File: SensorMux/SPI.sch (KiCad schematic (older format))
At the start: 12 parts

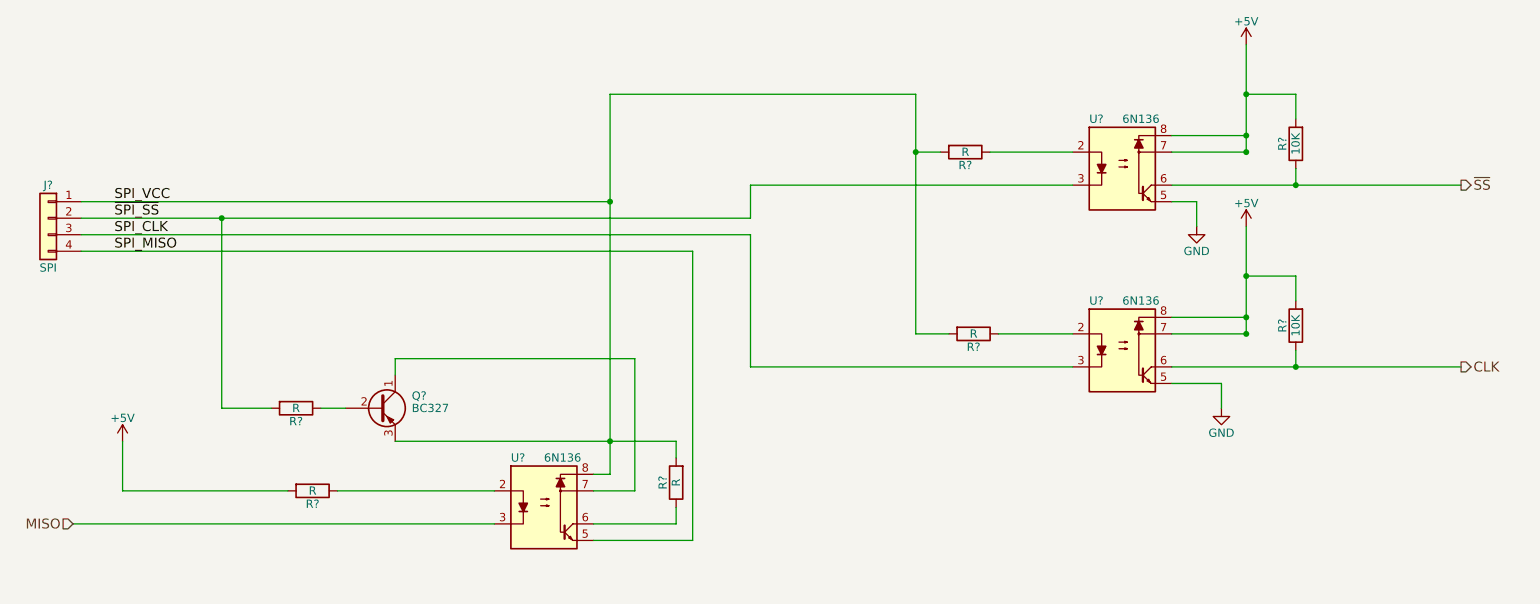
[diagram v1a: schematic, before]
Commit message: Working on adding analog part with SPI adjustment so the computer can control the opamps without needing manual trimpots.
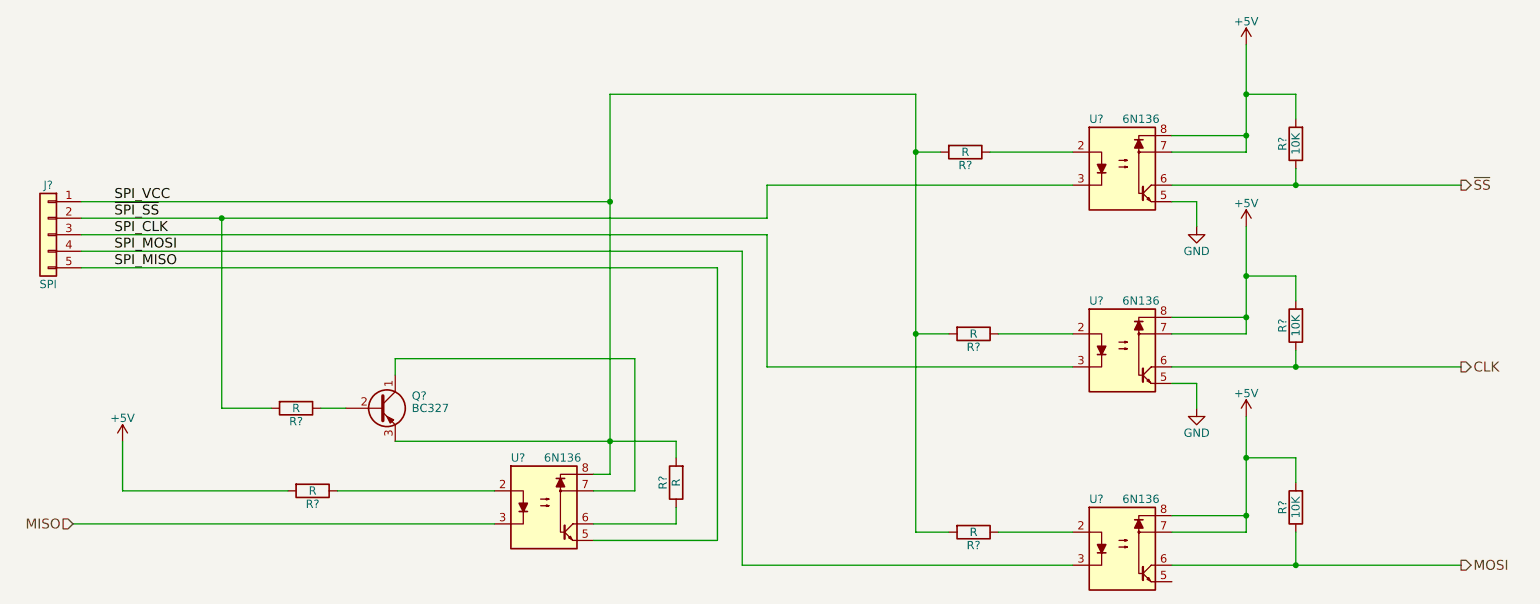
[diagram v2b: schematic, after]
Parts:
- removed J?: SPI, symbol Conn_01x04
- added J?: SPI, symbol Conn_01x05
- added R?: R, symbol R
- added R?: 10K, symbol R
- added U?: 6N136, Housings_DIP:DIP-8_W7.62mm, symbol 6N136
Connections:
- net +5V: now also R?.2, U?.7, U?.8
- net SPI_CLK: now also J?.3 (Pin_3)
- net SPI_MISO: now also J?.5 (Pin_5)
- net SPI_VCC: now also J?.1 (Pin_1), R?.2
- net ~SPI_SS: now also J?.2 (Pin_2)
- new net: R?.1, U?.2
- new net MOSI: R?.1, U?.6
- new net SPI_MOSI: J?.4 (Pin_4), U?.3
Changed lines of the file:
@@
-$EndComp
-$Comp
-L Conn_01x04 J?
-U 1 1 5A4AA249
-P 1700 3400
-F 0 "J?" H 1700 3600 50  0000 C CNN
-F 1 "SPI" H 1700 3100 50  0000 C CNN
-F 2 "" H 1700 3400 50  0001 C CNN
-F 3 "" H 1700 3400 50  0001 C CNN
-	1    1700 3400
-	-1   0    0    -1
 $EndComp
 $Comp
@@
 	-1   0    0    1
 $EndComp
-Text Label 2100 3600 0    60   ~ 0
+Text Label 2100 3700 0    60   ~ 0
 SPI_MISO
 $Comp
@@
 	7400 3000 7900 3000
 Wire Wire Line
-	5950 3200 7900 3200
+	6050 3200 7900 3200
 Wire Wire Line
 	1900 3300 5100 3300
@@
 	5100 2650 6950 2650
 Wire Wire Line
-	6950 2650 6950 4100
+	6950 2650 6950 5300
 Wire Wire Line
 	6950 4100 7150 4100
@@
 Connection ~ 6950 3000
 Wire Wire Line
-	5950 3400 5950 3200
-Wire Wire Line
-	1900 3400 5950 3400
-Wire Wire Line
-	1900 3500 5950 3500
-Wire Wire Line
-	5950 3500 5950 4300
-Wire Wire Line
-	5950 4300 7900 4300
+	6050 3400 6050 3200
+Wire Wire Line
+	1900 3400 6050 3400
+Wire Wire Line
+	1900 3500 6050 3500
+Wire Wire Line
+	6050 3500 6050 4300
+Wire Wire Line
+	6050 4300 7900 4300
 Wire Wire Line
 	3050 4550 2750 4550
@@
 	5500 5250 5500 5150
 Wire Wire Line
-	5000 5350 5600 5350
-Wire Wire Line
-	5600 5350 5600 3600
-Wire Wire Line
-	5600 3600 1900 3600
+	5000 5350 5750 5350
+Wire Wire Line
+	5750 5350 5750 3700
+Wire Wire Line
+	5750 3700 1900 3700
 Wire Wire Line
 	3450 5050 4400 5050
@@
 Wire Wire Line
 	8500 3200 10250 3200
-Connection ~ 8950 3000
 Wire Wire Line
 	8500 3300 8650 3300
@@
 L GND #PWR?
 U 1 1 5A4AAE1E
-P 8800 4550
-F 0 "#PWR?" H 8800 4300 50  0001 C CNN
-F 1 "GND" H 8800 4400 50  0000 C CNN
-F 2 "" H 8800 4550 50  0001 C CNN
-F 3 "" H 8800 4550 50  0001 C CNN
-	1    8800 4550
+P 8650 4550
+F 0 "#PWR?" H 8650 4300 50  0001 C CNN
+F 1 "GND" H 8650 4400 50  0000 C CNN
+F 2 "" H 8650 4550 50  0001 C CNN
+F 3 "" H 8650 4550 50  0001 C CNN
+	1    8650 4550
 	1    0    0    -1
 $EndComp
@@
 Wire Wire Line
 	8500 4300 10250 4300
-Connection ~ 8950 4100
-Wire Wire Line
-	8500 4400 8800 4400
-Wire Wire Line
-	8800 4400 8800 4550
+Wire Wire Line
+	8500 4400 8650 4400
+Wire Wire Line
+	8650 4400 8650 4550
 Wire Wire Line
 	8950 3450 8950 4100
@@
 Text HLabel 10250 4300 2    60   Output ~ 0
 CLK
+$Comp
+L Conn_01x05 J?
+U 1 1 5A5A91BD
+P 1700 3500
+F 0 "J?" H 1700 3800 50  0000 C CNN
+F 1 "SPI" H 1700 3200 50  0000 C CNN
+F 2 "" H 1700 3500 50  0001 C CNN
+F 3 "" H 1700 3500 50  0001 C CNN
+	1    1700 3500
+	-1   0    0    -1
+$EndComp
+Wire Wire Line
+	1900 3600 5900 3600
+Wire Wire Line
+	5900 3600 5900 5500
+$Comp
+L R R?
+U 1 1 5A5A9355
+P 7300 5300
+F 0 "R?" V 7380 5300 50  0000 C CNN
+F 1 "R" V 7300 5300 50  0000 C CNN
+F 2 "" V 7230 5300 50  0001 C CNN
+F 3 "" H 7300 5300 50  0001 C CNN
+	1    7300 5300
+	0    1    1    0
+$EndComp
+$Comp
+L 6N136 U?
+U 1 1 5A5A93D6
+P 8200 5400
+F 0 "U?" H 8000 5700 50  0000 L CNN
+F 1 "6N136" H 8200 5700 50  0000 L CNN
+F 2 "Housings_DIP:DIP-8_W7.62mm" H 8000 5100 50  0001 L CIN
+F 3 "" H 8200 5400 50  0001 L CNN
+	1    8200 5400
+	1    0    0    -1
+$EndComp
+Wire Wire Line
+	6950 5300 7150 5300
+Connection ~ 6950 4100
+Wire Wire Line
+	7450 5300 7900 5300
+Wire Wire Line
+	5900 5500 7900 5500
+Wire Wire Line
+	8950 5200 8500 5200
+Wire Wire Line
+	8950 4600 8950 5300
+$Comp
+L +5V #PWR?
+U 1 1 5A5A99E7
+P 8950 4600
+F 0 "#PWR?" H 8950 4450 50  0001 C CNN
+F 1 "+5V" H 8950 4740 50  0000 C CNN
+F 2 "" H 8950 4600 50  0001 C CNN
+F 3 "" H 8950 4600 50  0001 C CNN
+	1    8950 4600
+	1    0    0    -1
+$EndComp
+Wire Wire Line
+	8500 5500 10250 5500
+Wire Wire Line
+	8950 5300 8500 5300
+Connection ~ 8950 5200
+$Comp
+L R R?
+U 1 1 5A5AA53A
+P 9250 5150
+F 0 "R?" V 9330 5150 50  0000 C CNN
+F 1 "10K" V 9250 5150 50  0000 C CNN
+F 2 "" V 9180 5150 50  0001 C CNN
+F 3 "" H 9250 5150 50  0001 C CNN
+	1    9250 5150
+	-1   0    0    1
+$EndComp
+Wire Wire Line
+	9250 5000 9250 4850
+Wire Wire Line
+	9250 4850 8950 4850
+Connection ~ 8950 4850
+Wire Wire Line
+	9250 5300 9250 5500
+Connection ~ 9250 5500
+Text HLabel 10250 5500 2    60   Output ~ 0
+MOSI
+Text Label 2100 3600 0    60   ~ 0
+SPI_MOSI
 $EndSCHEMATC
